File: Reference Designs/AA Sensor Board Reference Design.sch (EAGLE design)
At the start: 21 parts, among them IC1 TPS62730, M2 AETHERMESH_MODULEMEZZ-HOLES

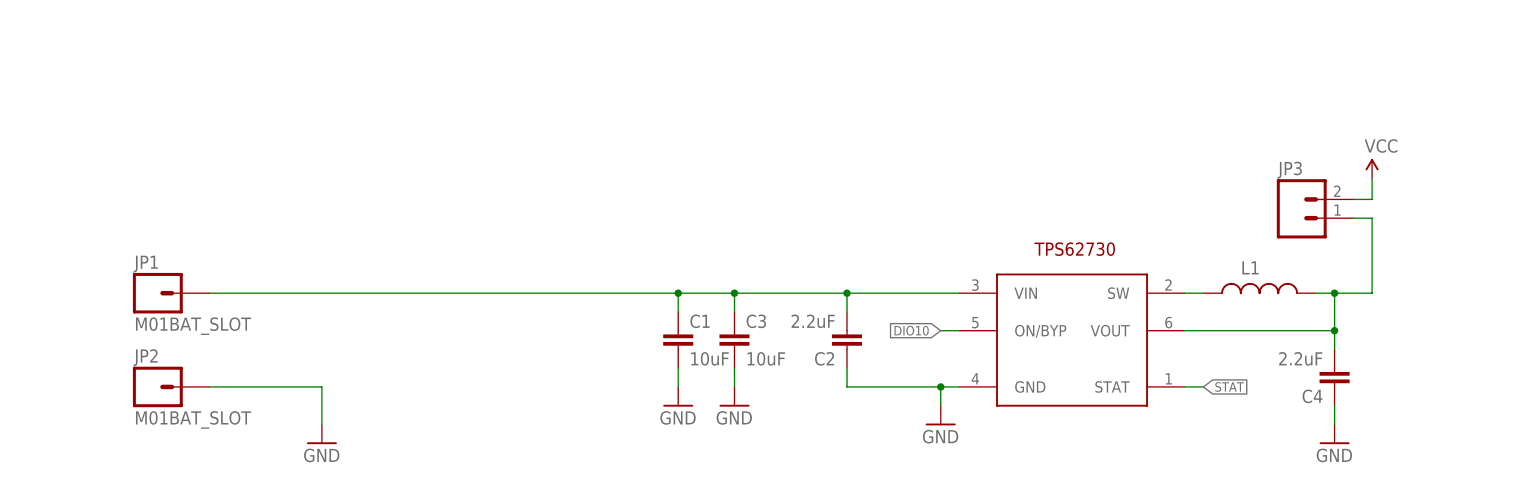
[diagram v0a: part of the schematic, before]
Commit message: Updated AA sensor board reference design
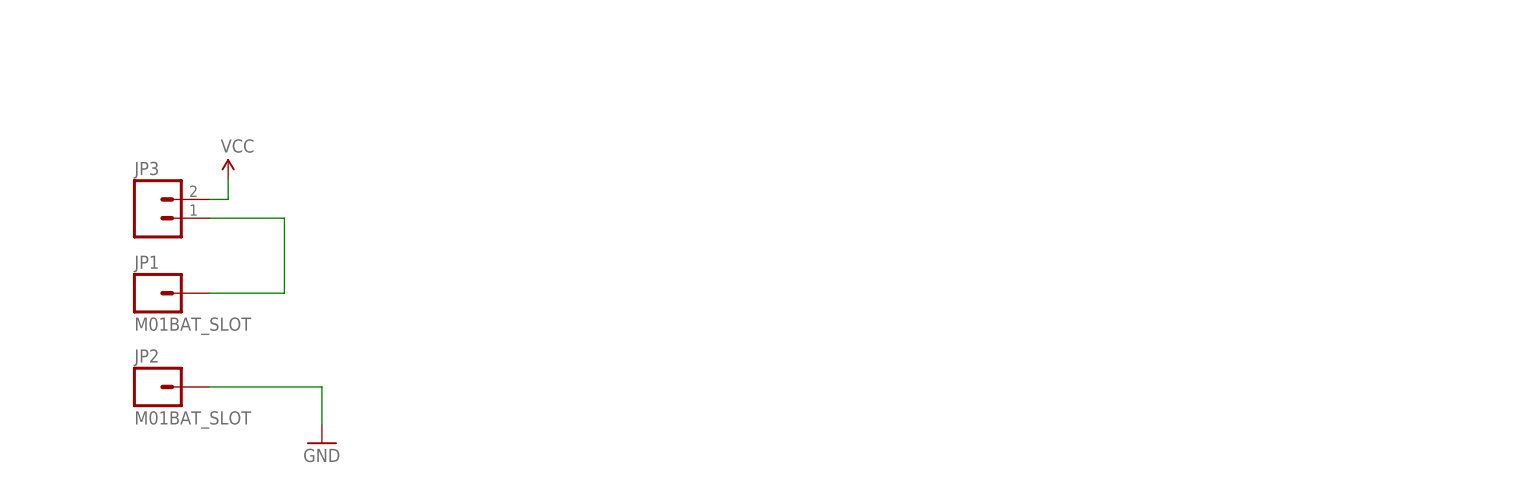
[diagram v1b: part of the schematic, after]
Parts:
- removed C1, C3: 10uF, 2. growflux:CAPC0805
- removed C2, C4: 2.2uF, 2. growflux:CAPC0402
- removed IC1: TPS62730, 3. growflux:TPS62730
- removed L1: 2.2uH, 2. growflux:INDUCTOR
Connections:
- removed net L1: IC1.SW, L1.1
- removed net STAT: IC1.STAT
- net DIO10: no longer IC1.ON/BYP
- net GND: no longer C1.2, C2.1, C3.2, C4.1, IC1.GND
- net N$4: now also JP1.1; no longer C4.2, IC1.VOUT, L1.2
- net VBAT: no longer C1.1, C2.2, C3.1, IC1.VIN, JP1.1
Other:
- moved on the sheet: JP3
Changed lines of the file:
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@@
 <?xml version="1.0" encoding="utf-8"?>
 <!DOCTYPE eagle SYSTEM "eagle.dtd">
-<eagle version="8.4.1">
+<eagle version="8.6.0">
 <drawing>
 <settings>
@@
 </part>
 <part name="GND1" library="3. growflux" library_urn="urn:adsk.eagle:library:207379" deviceset="GND" device=""/>
-<part name="C1" library="2. growflux" deviceset="CAP" device="C0805" value="10uF">
-<attribute name="ALT#" value="GRM21BR71A106MA73L"/>
-<attribute name="MFG#" value="MF-CAP-1206-10UF"/>
-</part>
-<part name="GND3" library="SparkFun-Aesthetics" deviceset="GND" device=""/>
-<part name="GND4" library="SparkFun-Aesthetics" deviceset="GND" device=""/>
-<part name="IC1" library="3. growflux" deviceset="TPS62730" device="" package3d_urn="urn:adsk.eagle:package:208239/1">
-<attribute name="MFG#" value="TPS62730DRYR"/>
-</part>
-<part name="L1" library="2. growflux" deviceset="INDUCTOR" device="" value="2.2uH">
-<attribute name="ALT#" value="CKP2012N2R2M-T"/>
-<attribute name="MFG#" value="LQM21PN2R2NGC"/>
-</part>
-<part name="C2" library="2. growflux" deviceset="CAP" device="C0402" value="2.2uF">
-<attribute name="ALT#" value="04026D225KAT2A"/>
-<attribute name="MFG#" value="CC0402KRX5R5BB225"/>
-</part>
-<part name="GND5" library="SparkFun-Aesthetics" deviceset="GND" device=""/>
-<part name="GND6" library="SparkFun-Aesthetics" deviceset="GND" device=""/>
-<part name="C3" library="2. growflux" deviceset="CAP" device="C0805" value="10uF">
-<attribute name="ALT#" value="GRM21BR71A106MA73L"/>
-<attribute name="MFG#" value="MF-CAP-1206-10UF"/>
-</part>
-<part name="C4" library="2. growflux" deviceset="CAP" device="C0402" value="2.2uF">
-<attribute name="ALT#" value="04026D225KAT2A"/>
-<attribute name="MFG#" value="CC0402KRX5R5BB225"/>
-</part>
 <part name="D2" library="MF_LEDs" deviceset="LED_RGB_CA" device="_PLCC4">
 <attribute name="MFG#" value="MF-LED-3228-RGB"/>
@@
 </instance>
 <instance part="GND1" gate="1" x="66.04" y="83.82"/>
-<instance part="C1" gate="G$1" x="86.36" y="20.32">
-<attribute name="ALT#" x="86.36" y="20.32" size="1.778" layer="96" display="off"/>
-<attribute name="MFG#" x="86.36" y="20.32" size="1.778" layer="96" display="off"/>
-</instance>
-<instance part="GND3" gate="1" x="93.98" y="12.7"/>
-<instance part="GND4" gate="1" x="86.36" y="12.7"/>
-<instance part="IC1" gate="G$1" x="139.7" y="17.78">
-<attribute name="MFG#" x="139.7" y="17.78" size="1.778" layer="96" display="off"/>
-</instance>
-<instance part="L1" gate="G$1" x="165.1" y="27.94" rot="R90">
-<attribute name="MFG#" x="165.1" y="27.94" size="1.778" layer="96" rot="R90" display="off"/>
-<attribute name="ALT#" x="165.1" y="27.94" size="1.778" layer="96" rot="R90" display="off"/>
-</instance>
-<instance part="C2" gate="G$1" x="109.22" y="22.86" rot="R180">
-<attribute name="MFG#" x="109.22" y="22.86" size="1.778" layer="96" rot="R180" display="off"/>
-<attribute name="ALT#" x="109.22" y="22.86" size="1.778" layer="96" rot="R180" display="off"/>
-</instance>
-<instance part="GND5" gate="1" x="121.92" y="10.16"/>
-<instance part="GND6" gate="1" x="175.26" y="7.62"/>
-<instance part="C3" gate="G$1" x="93.98" y="20.32">
-<attribute name="ALT#" x="93.98" y="20.32" size="1.778" layer="96" display="off"/>
-<attribute name="MFG#" x="93.98" y="20.32" size="1.778" layer="96" display="off"/>
-</instance>
-<instance part="C4" gate="G$1" x="175.26" y="17.78" rot="R180">
-<attribute name="MFG#" x="175.26" y="17.78" size="1.778" layer="96" rot="R180" display="off"/>
-<attribute name="ALT#" x="175.26" y="17.78" size="1.778" layer="96" rot="R180" display="off"/>
-</instance>
 <instance part="D2" gate="G$1" x="165.1" y="132.08"/>
 <instance part="SUPPLY4" gate="G$1" x="152.4" y="137.16"/>
@@
 </instance>
 <instance part="U$2" gate="G$1" x="-5.08" y="88.9"/>
-<instance part="JP3" gate="G$1" x="170.18" y="38.1"/>
-<instance part="SUPPLY6" gate="G$1" x="180.34" y="43.434"/>
+<instance part="JP3" gate="G$1" x="15.24" y="38.1"/>
+<instance part="SUPPLY6" gate="G$1" x="25.4" y="43.434"/>
 <instance part="TC2" gate="A" x="259.08" y="45.72"/>
 <instance part="GND9" gate="1" x="281.94" y="30.48"/>
@@
 </segment>
 <segment>
-<wire x1="93.98" y1="15.24" x2="93.98" y2="17.78" width="0.1524" layer="91"/>
-<pinref part="GND3" gate="1" pin="GND"/>
-<pinref part="C3" gate="G$1" pin="2"/>
-</segment>
-<segment>
-<pinref part="C1" gate="G$1" pin="2"/>
-<wire x1="86.36" y1="15.24" x2="86.36" y2="17.78" width="0.1524" layer="91"/>
-<pinref part="GND4" gate="1" pin="GND"/>
-</segment>
-<segment>
-<pinref part="C2" gate="G$1" pin="1"/>
-<wire x1="109.22" y1="17.78" x2="109.22" y2="15.24" width="0.1524" layer="91"/>
-<pinref part="GND5" gate="1" pin="GND"/>
-<wire x1="109.22" y1="15.24" x2="121.92" y2="15.24" width="0.1524" layer="91"/>
-<wire x1="121.92" y1="15.24" x2="121.92" y2="12.7" width="0.1524" layer="91"/>
-<pinref part="IC1" gate="G$1" pin="GND"/>
-<wire x1="121.92" y1="15.24" x2="124.46" y2="15.24" width="0.1524" layer="91"/>
-<junction x="121.92" y="15.24"/>
-</segment>
-<segment>
-<pinref part="GND6" gate="1" pin="GND"/>
-<wire x1="175.26" y1="10.16" x2="175.26" y2="12.7" width="0.1524" layer="91"/>
-<pinref part="C4" gate="G$1" pin="1"/>
-</segment>
-<segment>
 <pinref part="JP2" gate="G$1" pin="1"/>
 <wire x1="22.86" y1="15.24" x2="38.1" y2="15.24" width="0.1524" layer="91"/>
@@
 <pinref part="JP3" gate="G$1" pin="2"/>
 <pinref part="SUPPLY6" gate="G$1" pin="VCC"/>
-<wire x1="177.8" y1="40.64" x2="180.34" y2="40.64" width="0.1524" layer="91"/>
-<wire x1="180.34" y1="40.64" x2="180.34" y2="43.434" width="0.1524" layer="91"/>
+<wire x1="22.86" y1="40.64" x2="25.4" y2="40.64" width="0.1524" layer="91"/>
+<wire x1="25.4" y1="40.64" x2="25.4" y2="43.434" width="0.1524" layer="91"/>
 </segment>
 <segment>
@@
 <net name="VBAT" class="0">
 <segment>
-<pinref part="IC1" gate="G$1" pin="VIN"/>
-<pinref part="C2" gate="G$1" pin="2"/>
-<wire x1="124.46" y1="27.94" x2="109.22" y2="27.94" width="0.1524" layer="91"/>
-<wire x1="109.22" y1="27.94" x2="109.22" y2="25.4" width="0.1524" layer="91"/>
-<junction x="109.22" y="27.94"/>
-<pinref part="C1" gate="G$1" pin="1"/>
-<wire x1="86.36" y1="27.94" x2="93.98" y2="27.94" width="0.1524" layer="91"/>
-<wire x1="93.98" y1="27.94" x2="109.22" y2="27.94" width="0.1524" layer="91"/>
-<wire x1="86.36" y1="25.4" x2="86.36" y2="27.94" width="0.1524" layer="91"/>
-<junction x="86.36" y="27.94"/>
-<wire x1="93.98" y1="25.4" x2="93.98" y2="27.94" width="0.1524" layer="91"/>
-<junction x="93.98" y="27.94"/>
-<pinref part="C3" gate="G$1" pin="1"/>
-<wire x1="86.36" y1="27.94" x2="22.86" y2="27.94" width="0.1524" layer="91"/>
-<pinref part="JP1" gate="G$1" pin="1"/>
-</segment>
-<segment>
 <pinref part="TC2" gate="A" pin="9"/>
 <wire x1="271.78" y1="50.8" x2="266.7" y2="50.8" width="0.1524" layer="91"/>
@@
 </segment>
 </net>
-<net name="L1" class="0">
-<segment>
-<pinref part="IC1" gate="G$1" pin="SW"/>
-<pinref part="L1" gate="G$1" pin="1"/>
-<wire x1="154.94" y1="27.94" x2="157.48" y2="27.94" width="0.1524" layer="91"/>
-</segment>
-</net>
-<net name="STAT" class="0">
-<segment>
-<pinref part="IC1" gate="G$1" pin="STAT"/>
-<wire x1="157.48" y1="15.24" x2="154.94" y2="15.24" width="0.1524" layer="91"/>
-<label x="157.48" y="15.24" size="1.27" layer="95" xref="yes"/>
-</segment>
-</net>
 <net name="DIO2" class="0">
 <segment>
@@
 <wire x1="48.26" y1="114.3" x2="53.34" y2="114.3" width="0.1524" layer="91"/>
 <label x="48.26" y="114.3" size="1.27" layer="95" rot="R180" xref="yes"/>
-</segment>
-<segment>
-<pinref part="IC1" gate="G$1" pin="ON/BYP"/>
-<wire x1="121.92" y1="22.86" x2="124.46" y2="22.86" width="0.1524" layer="91"/>
-<label x="121.92" y="22.86" size="1.27" layer="95" rot="R180" xref="yes"/>
 </segment>
 <segment>
@@
 <net name="N$4" class="0">
 <segment>
-<pinref part="IC1" gate="G$1" pin="VOUT"/>
-<wire x1="154.94" y1="22.86" x2="175.26" y2="22.86" width="0.1524" layer="91"/>
-<wire x1="175.26" y1="22.86" x2="175.26" y2="27.94" width="0.1524" layer="91"/>
-<pinref part="L1" gate="G$1" pin="2"/>
-<wire x1="172.72" y1="27.94" x2="175.26" y2="27.94" width="0.1524" layer="91"/>
-<wire x1="175.26" y1="27.94" x2="180.34" y2="27.94" width="0.1524" layer="91"/>
-<junction x="175.26" y="27.94"/>
-<wire x1="175.26" y1="20.32" x2="175.26" y2="22.86" width="0.1524" layer="91"/>
-<junction x="175.26" y="22.86"/>
-<pinref part="C4" gate="G$1" pin="2"/>
 <pinref part="JP3" gate="G$1" pin="1"/>
-<wire x1="177.8" y1="38.1" x2="180.34" y2="38.1" width="0.1524" layer="91"/>
-<wire x1="180.34" y1="27.94" x2="180.34" y2="38.1" width="0.1524" layer="91"/>
-</segment>
-</net>
+<wire x1="22.86" y1="38.1" x2="33.02" y2="38.1" width="0.1524" layer="91"/>
+<pinref part="JP1" gate="G$1" pin="1"/>
+<wire x1="22.86" y1="27.94" x2="33.02" y2="27.94" width="0.1524" layer="91"/>
+<wire x1="33.02" y1="27.94" x2="33.02" y2="38.1" width="0.1524" layer="91"/>
+</segment>
+</net>
